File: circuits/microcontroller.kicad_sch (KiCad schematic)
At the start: 13 parts, among them U14 ESP32-WROOM-32

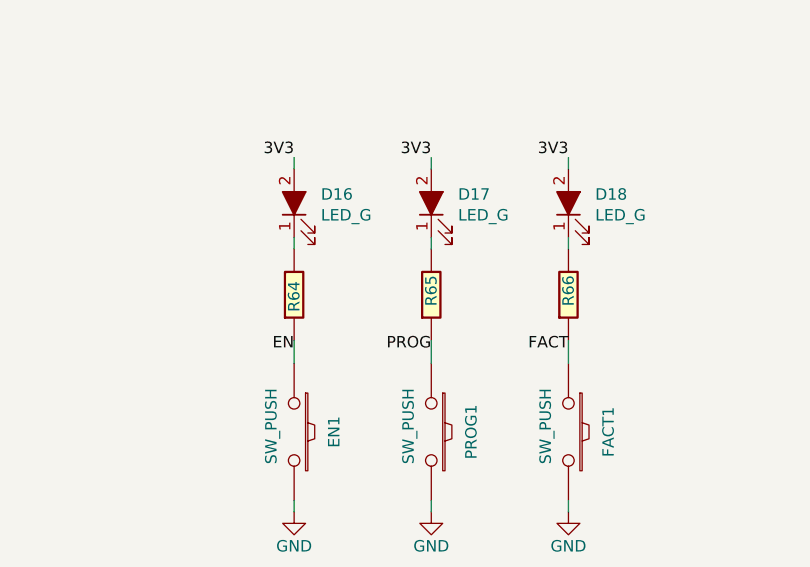
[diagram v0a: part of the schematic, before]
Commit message: corrected footprints for manufacturer
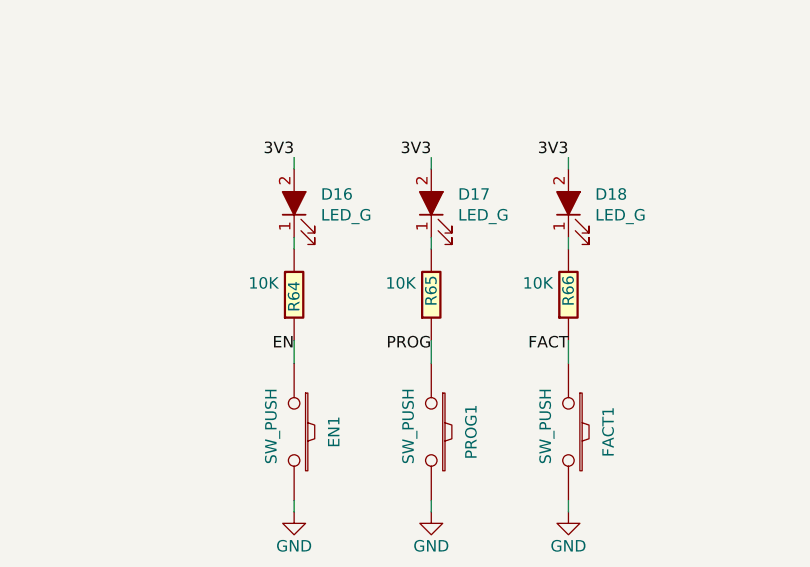
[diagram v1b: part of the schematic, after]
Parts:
- R64, R65, R66: value (none) -> 10K; footprint (none) -> Resistor_SMD:R_0402_1005Metric_Pad0.72x0.64mm_HandSolder
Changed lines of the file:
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@@
       (effects (font (size 1.27 1.27)) (justify left))
     )
-    (property "Value" "" (id 1) (at 86.36 104.14 0)
+    (property "Value" "10K" (id 1) (at 86.36 104.14 0)
       (effects (font (size 1.27 1.27)) (justify left))
     )
-    (property "Footprint" "" (id 2) (at 89.662 105.41 90)
+    (property "Footprint" "Resistor_SMD:R_0402_1005Metric_Pad0.72x0.64mm_HandSolder" (id 2) (at 89.662 105.41 90)
       (effects (font (size 1.27 1.27)) hide)
     )
@@
       (effects (font (size 1.27 1.27)) (justify left))
     )
-    (property "Value" "" (id 1) (at 101.6 104.14 0)
+    (property "Value" "10K" (id 1) (at 101.6 104.14 0)
       (effects (font (size 1.27 1.27)) (justify left))
     )
-    (property "Footprint" "" (id 2) (at 104.902 105.41 90)
+    (property "Footprint" "Resistor_SMD:R_0402_1005Metric_Pad0.72x0.64mm_HandSolder" (id 2) (at 104.902 105.41 90)
       (effects (font (size 1.27 1.27)) hide)
     )
@@
       (effects (font (size 1.27 1.27)) (justify left))
     )
-    (property "Value" "" (id 1) (at 116.84 104.14 0)
+    (property "Value" "10K" (id 1) (at 116.84 104.14 0)
       (effects (font (size 1.27 1.27)) (justify left))
     )
-    (property "Footprint" "" (id 2) (at 120.142 105.41 90)
+    (property "Footprint" "Resistor_SMD:R_0402_1005Metric_Pad0.72x0.64mm_HandSolder" (id 2) (at 120.142 105.41 90)
       (effects (font (size 1.27 1.27)) hide)
     )
